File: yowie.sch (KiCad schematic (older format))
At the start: 50 parts

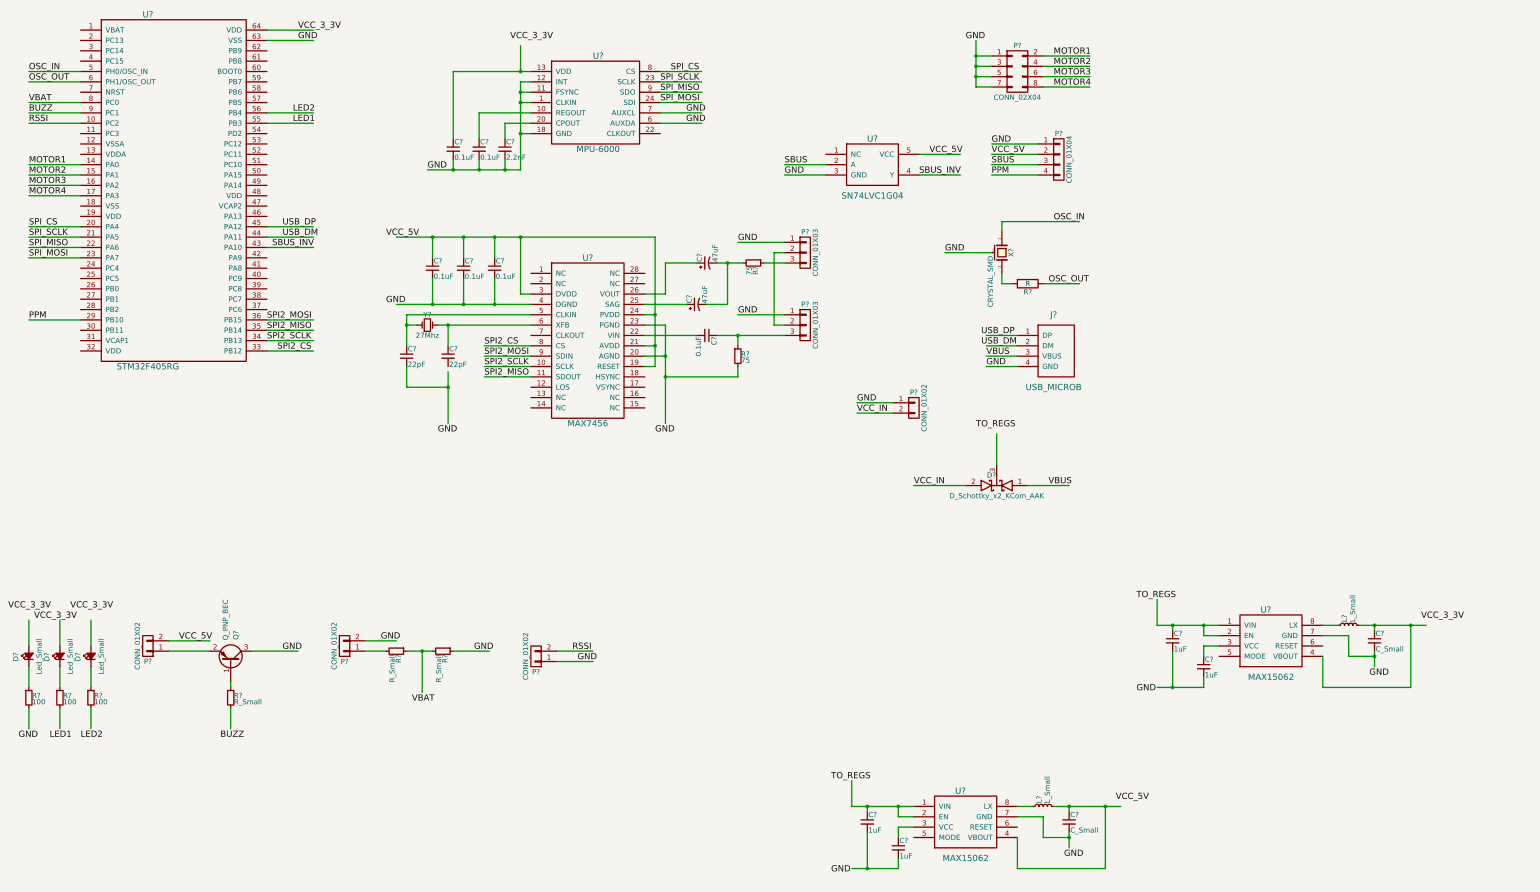
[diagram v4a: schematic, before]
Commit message: Unified VBAT and VCC_IN
Resolves #2
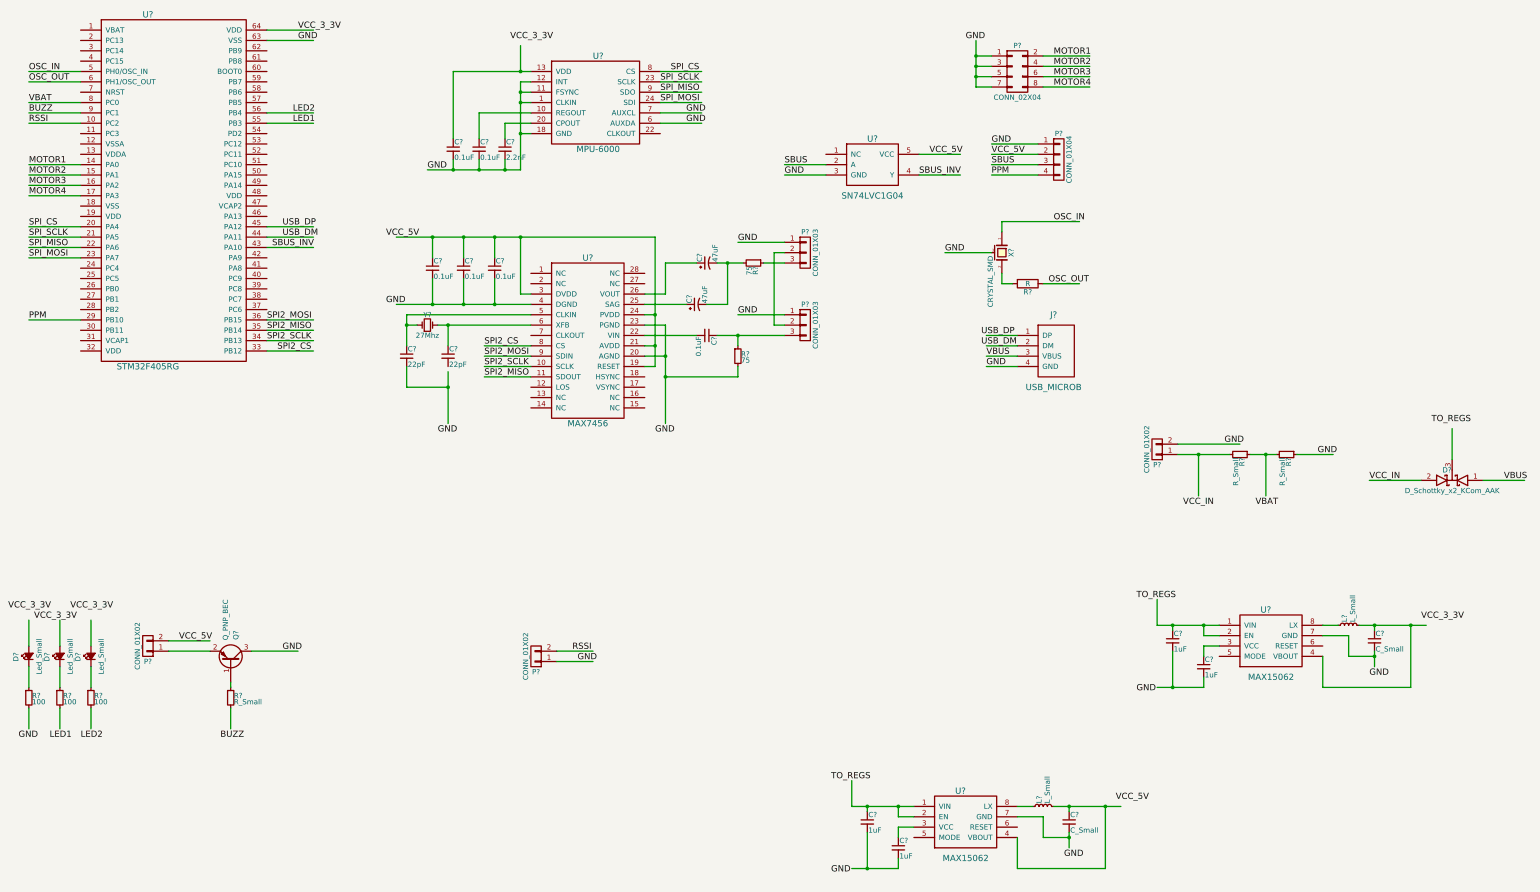
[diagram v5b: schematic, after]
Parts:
- removed P?: CONN_01X02, symbol CONN_01X02
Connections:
- wire segments 226 -> 186
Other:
- moved on the sheet: D?, P?, R?
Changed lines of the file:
@@
 L D_Schottky_x2_KCom_AAK D?
 U 1 1 56526B1B
-P 10200 5150
-F 0 "D?" H 10250 5050 50  0000 C CNN
-F 1 "D_Schottky_x2_KCom_AAK" H 10200 5250 50  0000 C CNN
-F 2 "" H 10200 5150 60  0000 C CNN
-F 3 "" H 10200 5150 60  0000 C CNN
-	1    10200 5150
+P 14600 5100
+F 0 "D?" H 14650 5000 50  0000 C CNN
+F 1 "D_Schottky_x2_KCom_AAK" H 14600 5200 50  0000 C CNN
+F 2 "" H 14600 5100 60  0000 C CNN
+F 3 "" H 14600 5100 60  0000 C CNN
+	1    14600 5100
 	-1   0    0    1
 $EndComp
 Text Label 10100 3900 0    60   ~ 0
 VBUS
-Text Label 10700 5150 0    60   ~ 0
+Text Label 15100 5100 0    60   ~ 0
 VBUS
-Text Label 10000 4600 0    60   ~ 0
+Text Label 14400 4550 0    60   ~ 0
 TO_REGS
 Text Label 10100 4000 0    60   ~ 0
@@
 Text Label 10750 2600 0    60   ~ 0
 OSC_IN
-$Comp
-L CONN_01X02 P?
-U 1 1 565D32F3
-P 9400 4400
-F 0 "P?" H 9400 4550 50  0000 C CNN
-F 1 "CONN_01X02" V 9500 4400 50  0000 C CNN
-F 2 "" H 9400 4400 60  0000 C CNN
-F 3 "" H 9400 4400 60  0000 C CNN
-	1    9400 4400
-	1    0    0    -1
-$EndComp
-Text Label 8850 4350 0    60   ~ 0
-GND
-Text Label 8850 4450 0    60   ~ 0
-VCC_IN
-Text Label 9400 5150 0    60   ~ 0
+Text Label 13800 5100 0    60   ~ 0
 VCC_IN
 $Comp
@@
 RSSI
 $Comp
-L CONN_01X02 P?
-U 1 1 56604F96
-P 3900 6700
-F 0 "P?" H 3900 6850 50  0000 C CNN
-F 1 "CONN_01X02" V 4000 6700 50  0000 C CNN
-F 2 "" H 3900 6700 60  0000 C CNN
-F 3 "" H 3900 6700 60  0000 C CNN
-	1    3900 6700
-	-1   0    0    1
-$EndComp
-$Comp
 L R_Small R?
 U 1 1 5660521D
-P 4400 6750
-F 0 "R?" H 4430 6770 50  0000 L CNN
-F 1 "R_Small" H 4430 6710 50  0000 L CNN
-F 2 "" H 4400 6750 60  0000 C CNN
-F 3 "" H 4400 6750 60  0000 C CNN
-	1    4400 6750
+P 12550 4850
+F 0 "R?" H 12580 4870 50  0000 L CNN
+F 1 "R_Small" H 12580 4810 50  0000 L CNN
+F 2 "" H 12550 4850 60  0000 C CNN
+F 3 "" H 12550 4850 60  0000 C CNN
+	1    12550 4850
 	0    1    1    0
 $EndComp
@@
 L R_Small R?
 U 1 1 566052CC
-P 4850 6750
-F 0 "R?" H 4880 6770 50  0000 L CNN
-F 1 "R_Small" H 4880 6710 50  0000 L CNN
-F 2 "" H 4850 6750 60  0000 C CNN
-F 3 "" H 4850 6750 60  0000 C CNN
-	1    4850 6750
+P 13000 4850
+F 0 "R?" H 13030 4870 50  0000 L CNN
+F 1 "R_Small" H 13030 4810 50  0000 L CNN
+F 2 "" H 13000 4850 60  0000 C CNN
+F 3 "" H 13000 4850 60  0000 C CNN
+	1    13000 4850
 	0    1    1    0
 $EndComp
-Text Label 4250 6650 0    60   ~ 0
-GND
-Text Label 5150 6750 0    60   ~ 0
-GND
-Text Label 4550 7250 0    60   ~ 0
+Text Label 12400 4750 0    60   ~ 0
+GND
+Text Label 13300 4850 0    60   ~ 0
+GND
+Text Label 12700 5350 0    60   ~ 0
 VBAT
 $Comp
@@
 $EndComp
 Wire Wire Line
-	5600 2100 5600 1750
-Wire Wire Line
-	5600 1750 5600 1450
-Wire Wire Line
-	5600 1450 5600 1350
-Wire Wire Line
-	5600 1350 5600 1250
+	5600 2100 5600 1250
 Connection ~ 5600 1350
 Wire Wire Line
@@
 Connection ~ 10000 1200
 Wire Wire Line
-	10000 850  10000 1000
-Wire Wire Line
-	10000 1000 10000 1100
-Wire Wire Line
-	10000 1100 10000 1200
-Wire Wire Line
-	10000 1200 10000 1300
+	10000 850  10000 1300
 Wire Wire Line
 	10000 1300 10150 1300
@@
 	10600 1850 10150 1850
 Wire Wire Line
-	9900 5150 9400 5150
-Wire Wire Line
-	9200 4450 8850 4450
-Wire Wire Line
-	9200 4350 8850 4350
+	14300 5100 13800 5100
 Wire Wire Line
 	10250 2600 11000 2600
@@
 	10400 3900 10100 3900
 Wire Wire Line
-	10500 5150 10900 5150
-Wire Wire Line
-	10200 4950 10200 4650
-Wire Wire Line
-	4700 2100 4950 2100
-Wire Wire Line
-	4950 2100 5200 2100
-Wire Wire Line
-	5200 2100 5450 2100
-Wire Wire Line
-	5450 2100 5600 2100
+	14900 5100 15300 5100
+Wire Wire Line
+	14600 4900 14600 4600
+Wire Wire Line
+	4700 2100 5600 2100
 Connection ~ 5600 1150
 Wire Wire Line
@@
 Connection ~ 5450 2100
 Wire Wire Line
-	4950 1150 5600 1150
-Wire Wire Line
-	5600 1150 5700 1150
+	4950 1150 5700 1150
 Wire Wire Line
 	4950 1150 4950 1800
@@
 	5700 4100 5250 4100
 Wire Wire Line
-	4800 3600 4900 3600
-Wire Wire Line
-	4900 3600 5700 3600
+	4800 3600 5700 3600
 Wire Wire Line
 	4900 3600 4900 3800
@@
 	4600 3600 4500 3600
 Wire Wire Line
-	4500 3500 4500 3600
-Wire Wire Line
-	4500 3600 4500 3800
+	4500 3500 4500 3800
 Wire Wire Line
 	5700 3500 4500 3500
 Connection ~ 4500 3600
 Wire Wire Line
-	4400 3400 4750 3400
-Wire Wire Line
-	4750 3400 5050 3400
-Wire Wire Line
-	5050 3400 5350 3400
-Wire Wire Line
-	5350 3400 5700 3400
-Wire Wire Line
-	4900 4050 4900 4200
-Wire Wire Line
-	4900 4200 4900 4550
+	4400 3400 5700 3400
+Wire Wire Line
+	4900 4050 4900 4550
 Wire Wire Line
 	4500 4000 4500 4200
@@
 	5600 3300 5600 2750
 Wire Wire Line
-	4400 2750 4750 2750
-Wire Wire Line
-	4750 2750 5050 2750
-Wire Wire Line
-	5050 2750 5350 2750
-Wire Wire Line
-	5350 2750 5600 2750
-Wire Wire Line
-	5600 2750 6900 2750
+	4400 2750 6900 2750
 Connection ~ 4750 2750
 Connection ~ 5050 2750
@@
 	6800 3500 6900 3500
 Wire Wire Line
-	6900 2750 6900 3500
-Wire Wire Line
-	6900 3500 6900 3800
-Wire Wire Line
-	6900 3800 6900 4000
+	6900 2750 6900 4000
 Connection ~ 5600 2750
 Wire Wire Line
@@
 	6800 3600 7000 3600
 Wire Wire Line
-	7000 3600 7000 3900
-Wire Wire Line
-	7000 3900 7000 4100
-Wire Wire Line
-	7000 4100 7000 4550
+	7000 3600 7000 4550
 Wire Wire Line
 	6800 3900 7000 3900
@@
 	6800 3700 7300 3700
 Wire Wire Line
-	7500 3700 7700 3700
-Wire Wire Line
-	7700 3700 8150 3700
+	7500 3700 8150 3700
 Wire Wire Line
 	7700 3800 7700 3700
@@
 	8150 3000 7950 3000
 Wire Wire Line
-	7750 3000 7600 3000
-Wire Wire Line
-	7600 3000 7500 3000
+	7500 3000 7750 3000
 Wire Wire Line
 	7300 3000 7000 3000
@@
 	1350 1650 850  1650
 Wire Wire Line
-	4100 6650 4400 6650
-Wire Wire Line
-	4100 6750 4300 6750
-Wire Wire Line
-	4500 6750 4650 6750
-Wire Wire Line
-	4650 6750 4750 6750
-Wire Wire Line
-	4650 6750 4650 7150
-Connection ~ 4650 6750
-Wire Wire Line
-	4950 6750 5300 6750
+	11950 4750 12550 4750
+Wire Wire Line
+	11950 4850 12450 4850
+Wire Wire Line
+	12650 4850 12900 4850
+Wire Wire Line
+	12800 4850 12800 5250
+Connection ~ 12800 4850
+Wire Wire Line
+	13100 4850 13450 4850
 Wire Wire Line
 	5950 6750 6300 6750
@@
 	5950 6850 6300 6850
 Wire Wire Line
-	12350 6500 12200 6500
-Wire Wire Line
-	12200 6500 11900 6500
-Wire Wire Line
-	11900 6500 11750 6500
+	11750 6500 12350 6500
 Wire Wire Line
 	11750 6500 11750 6250
@@
 	12200 6700 12350 6700
 Wire Wire Line
-	12200 7000 12200 7100
-Wire Wire Line
-	12200 7100 11900 7100
-Wire Wire Line
-	11900 7100 11750 7100
+	12200 7100 12200 7000
+Wire Wire Line
+	11750 7100 12200 7100
 Wire Wire Line
 	11900 6750 11900 7100
@@
 $EndComp
 Wire Wire Line
-	13700 6500 13850 6500
-Wire Wire Line
-	13850 6500 14200 6500
-Wire Wire Line
-	14200 6500 14350 6500
+	13700 6500 14350 6500
 $Comp
 L C_Small C?
@@
 Connection ~ 14200 6500
 Wire Wire Line
-	13850 6750 13850 6800
-Wire Wire Line
-	13850 6800 13850 6900
+	13850 6750 13850 6900
 Text Label 13800 7000 0    60   ~ 0
 GND
@@
 $EndComp
 Wire Wire Line
-	9400 8250 9250 8250
-Wire Wire Line
-	9250 8250 8950 8250
-Wire Wire Line
-	8950 8250 8800 8250
+	8800 8250 9400 8250
 Wire Wire Line
 	8800 8250 8800 8000
@@
 	9250 8450 9400 8450
 Wire Wire Line
-	9250 8750 9250 8850
-Wire Wire Line
-	9250 8850 8950 8850
-Wire Wire Line
-	8950 8850 8800 8850
+	9250 8850 9250 8750
+Wire Wire Line
+	8800 8850 9250 8850
 Wire Wire Line
 	8950 8500 8950 8850
@@
 $EndComp
 Wire Wire Line
-	10750 8250 10900 8250
-Wire Wire Line
-	10900 8250 11250 8250
-Wire Wire Line
-	11250 8250 11400 8250
+	10750 8250 11400 8250
 $Comp
 L C_Small C?
@@
 Connection ~ 11250 8250
 Wire Wire Line
-	10900 8500 10900 8550
-Wire Wire Line
-	10900 8550 10900 8650
+	10900 8500 10900 8650
 Text Label 10850 8750 0    60   ~ 0
 GND
@@
 Text Label 11350 8200 0    60   ~ 0
 VCC_5V
+$Comp
+L CONN_01X02 P?
+U 1 1 56604F96
+P 11750 4800
+F 0 "P?" H 11750 4950 50  0000 C CNN
+F 1 "CONN_01X02" V 11850 4800 50  0000 C CNN
+F 2 "" H 11750 4800 60  0000 C CNN
+F 3 "" H 11750 4800 60  0000 C CNN
+	1    11750 4800
+	-1   0    0    1
+$EndComp
+Wire Wire Line
+	12150 4850 12150 5250
+Connection ~ 12150 4850
+Text Label 12000 5350 0    60   ~ 0
+VCC_IN
 $EndSCHEMATC

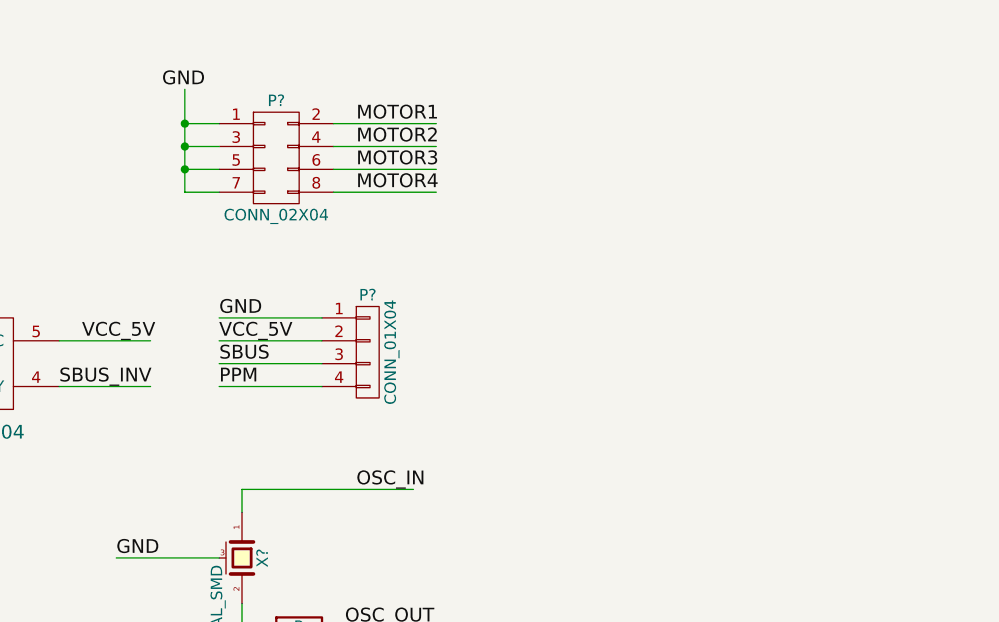
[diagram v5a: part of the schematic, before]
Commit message: Split ESC output connectors
Resolves #4
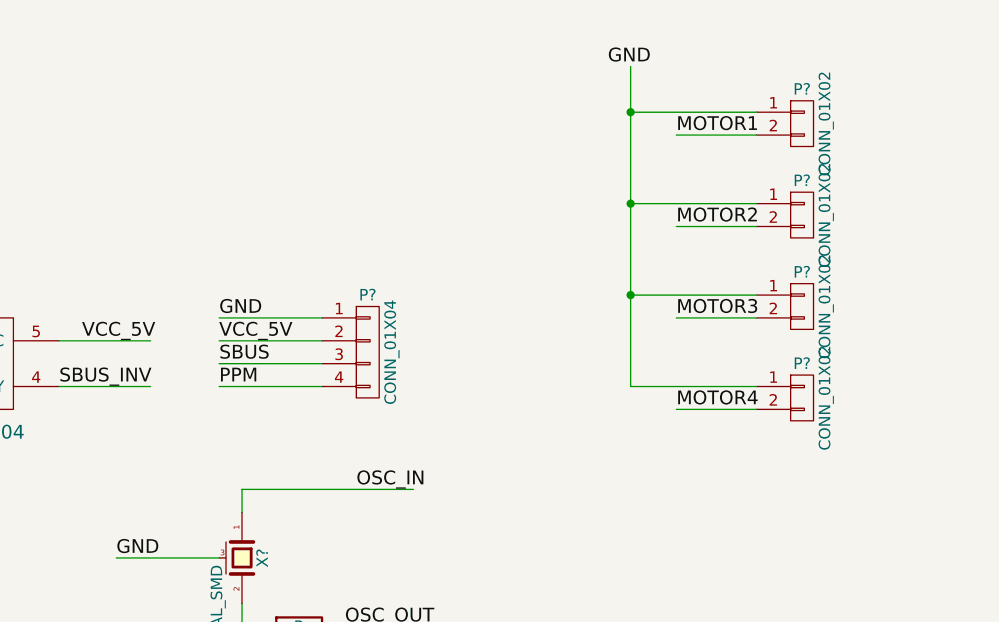
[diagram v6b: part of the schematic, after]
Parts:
- removed P?: CONN_02X04, symbol CONN_02X04
- added P? (x4): CONN_01X02, symbol CONN_01X02
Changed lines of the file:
@@
 Text Label 3200 2850 0    60   ~ 0
 SBUS_INV
-$Comp
-L CONN_02X04 P?
-U 1 1 565D4175
-P 10400 1150
-F 0 "P?" H 10400 1400 50  0000 C CNN
-F 1 "CONN_02X04" H 10400 900 50  0000 C CNN
-F 2 "" H 10400 -50 60  0000 C CNN
-F 3 "" H 10400 -50 60  0000 C CNN
-	1    10400 1150
-	1    0    0    -1
-$EndComp
-Text Label 9900 850  0    60   ~ 0
-GND
-Text Label 10750 1000 0    60   ~ 0
-MOTOR1
-Text Label 10750 1100 0    60   ~ 0
-MOTOR2
-Text Label 10750 1200 0    60   ~ 0
-MOTOR3
-Text Label 10750 1300 0    60   ~ 0
-MOTOR4
 Text Label 850  2050 0    60   ~ 0
 MOTOR1
@@
 Wire Wire Line
 	1350 2050 850  2050
-Connection ~ 10000 1000
-Connection ~ 10000 1100
-Connection ~ 10000 1200
-Wire Wire Line
-	10000 850  10000 1300
-Wire Wire Line
-	10000 1300 10150 1300
-Wire Wire Line
-	10150 1200 10000 1200
-Wire Wire Line
-	10150 1100 10000 1100
-Wire Wire Line
-	10150 1000 10000 1000
-Wire Wire Line
-	10650 1300 11100 1300
-Wire Wire Line
-	10650 1200 11100 1200
-Wire Wire Line
-	10650 1100 11100 1100
-Wire Wire Line
-	10650 1000 11100 1000
 Wire Wire Line
 	3150 2850 3600 2850
@@
 Text Label 12000 5350 0    60   ~ 0
 VCC_IN
+$Comp
+L CONN_01X02 P?
+U 1 1 56695EBB
+P 12700 1000
+F 0 "P?" H 12700 1150 50  0000 C CNN
+F 1 "CONN_01X02" V 12800 1000 50  0000 C CNN
+F 2 "" H 12700 1000 60  0000 C CNN
+F 3 "" H 12700 1000 60  0000 C CNN
+	1    12700 1000
+	1    0    0    -1
+$EndComp
+$Comp
+L CONN_01X02 P?
+U 1 1 56695F77
+P 12700 1400
+F 0 "P?" H 12700 1550 50  0000 C CNN
+F 1 "CONN_01X02" V 12800 1400 50  0000 C CNN
+F 2 "" H 12700 1400 60  0000 C CNN
+F 3 "" H 12700 1400 60  0000 C CNN
+	1    12700 1400
+	1    0    0    -1
+$EndComp
+$Comp
+L CONN_01X02 P?
+U 1 1 5669603A
+P 12700 1800
+F 0 "P?" H 12700 1950 50  0000 C CNN
+F 1 "CONN_01X02" V 12800 1800 50  0000 C CNN
+F 2 "" H 12700 1800 60  0000 C CNN
+F 3 "" H 12700 1800 60  0000 C CNN
+	1    12700 1800
+	1    0    0    -1
+$EndComp
+$Comp
+L CONN_01X02 P?
+U 1 1 566960FC
+P 12700 2200
+F 0 "P?" H 12700 2350 50  0000 C CNN
+F 1 "CONN_01X02" V 12800 2200 50  0000 C CNN
+F 2 "" H 12700 2200 60  0000 C CNN
+F 3 "" H 12700 2200 60  0000 C CNN
+	1    12700 2200
+	1    0    0    -1
+$EndComp
+Wire Wire Line
+	12500 950  11950 950
+Wire Wire Line
+	11950 750  11950 2150
+Wire Wire Line
+	11950 1350 12500 1350
+Connection ~ 11950 950
+Wire Wire Line
+	11950 1750 12500 1750
+Connection ~ 11950 1350
+Wire Wire Line
+	11950 2150 12500 2150
+Connection ~ 11950 1750
+Wire Wire Line
+	12500 1050 12150 1050
+Wire Wire Line
+	12500 1450 12150 1450
+Wire Wire Line
+	12500 1850 12150 1850
+Wire Wire Line
+	12500 2250 12150 2250
+Text Label 12150 1050 0    60   ~ 0
+MOTOR1
+Text Label 12150 1450 0    60   ~ 0
+MOTOR2
+Text Label 12150 1850 0    60   ~ 0
+MOTOR3
+Text Label 12150 2250 0    60   ~ 0
+MOTOR4
+Text Label 11850 750  0    60   ~ 0
+GND
 $EndSCHEMATC

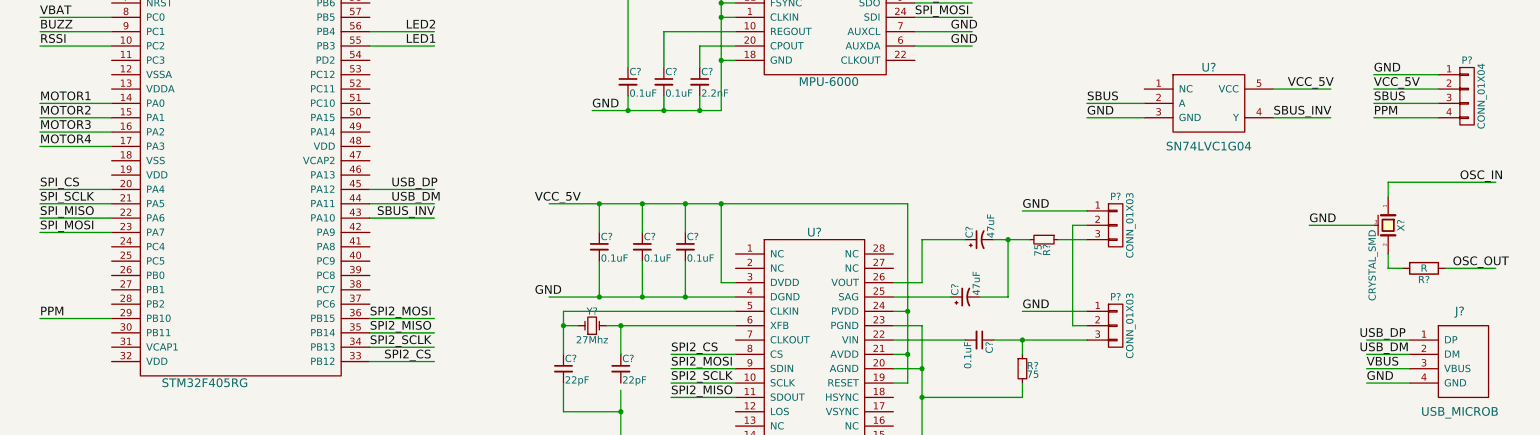
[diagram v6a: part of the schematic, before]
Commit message: Merged PPM and SAT pins
Resolves #5
Resolves #9
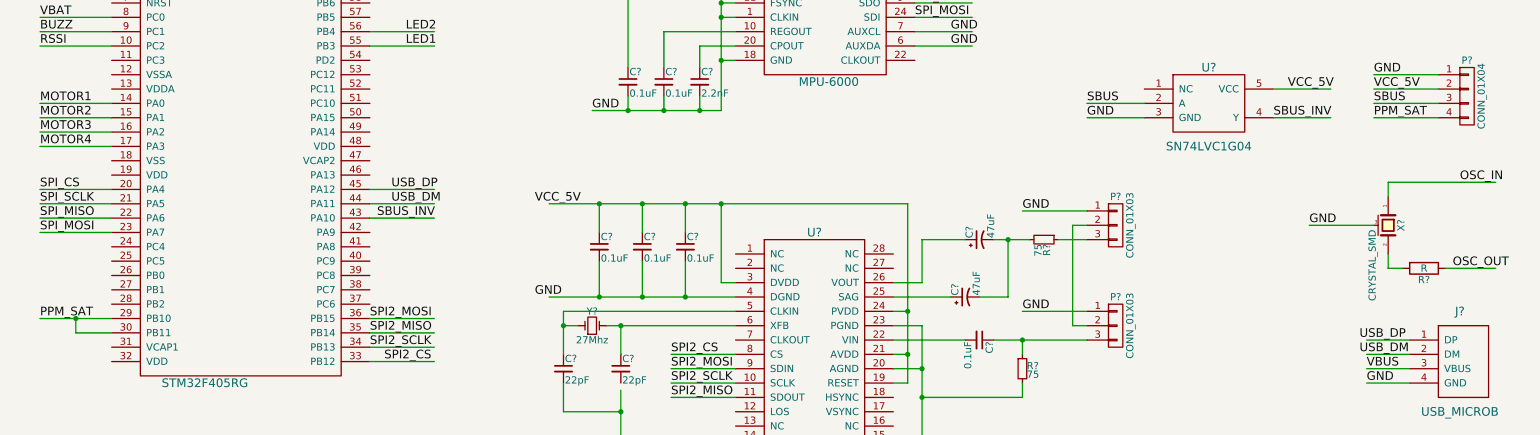
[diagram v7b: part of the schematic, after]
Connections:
- net labels added: PPM_SAT
- net labels removed: PPM
- wire segments 186 -> 188
